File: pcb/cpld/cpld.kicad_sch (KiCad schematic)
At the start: 29 parts, among them J1 Micro_SD_Card_Det1, J2 Bus_ISA_8bit_AB_Rev0, J3 Atmel-JTAG-10, SW1 ADDR SEL, U1 ATF1504AS-xJx44, U2 AMS1117-3.3, U3 74LVC125, U4 74HCT688, X1 16MHz

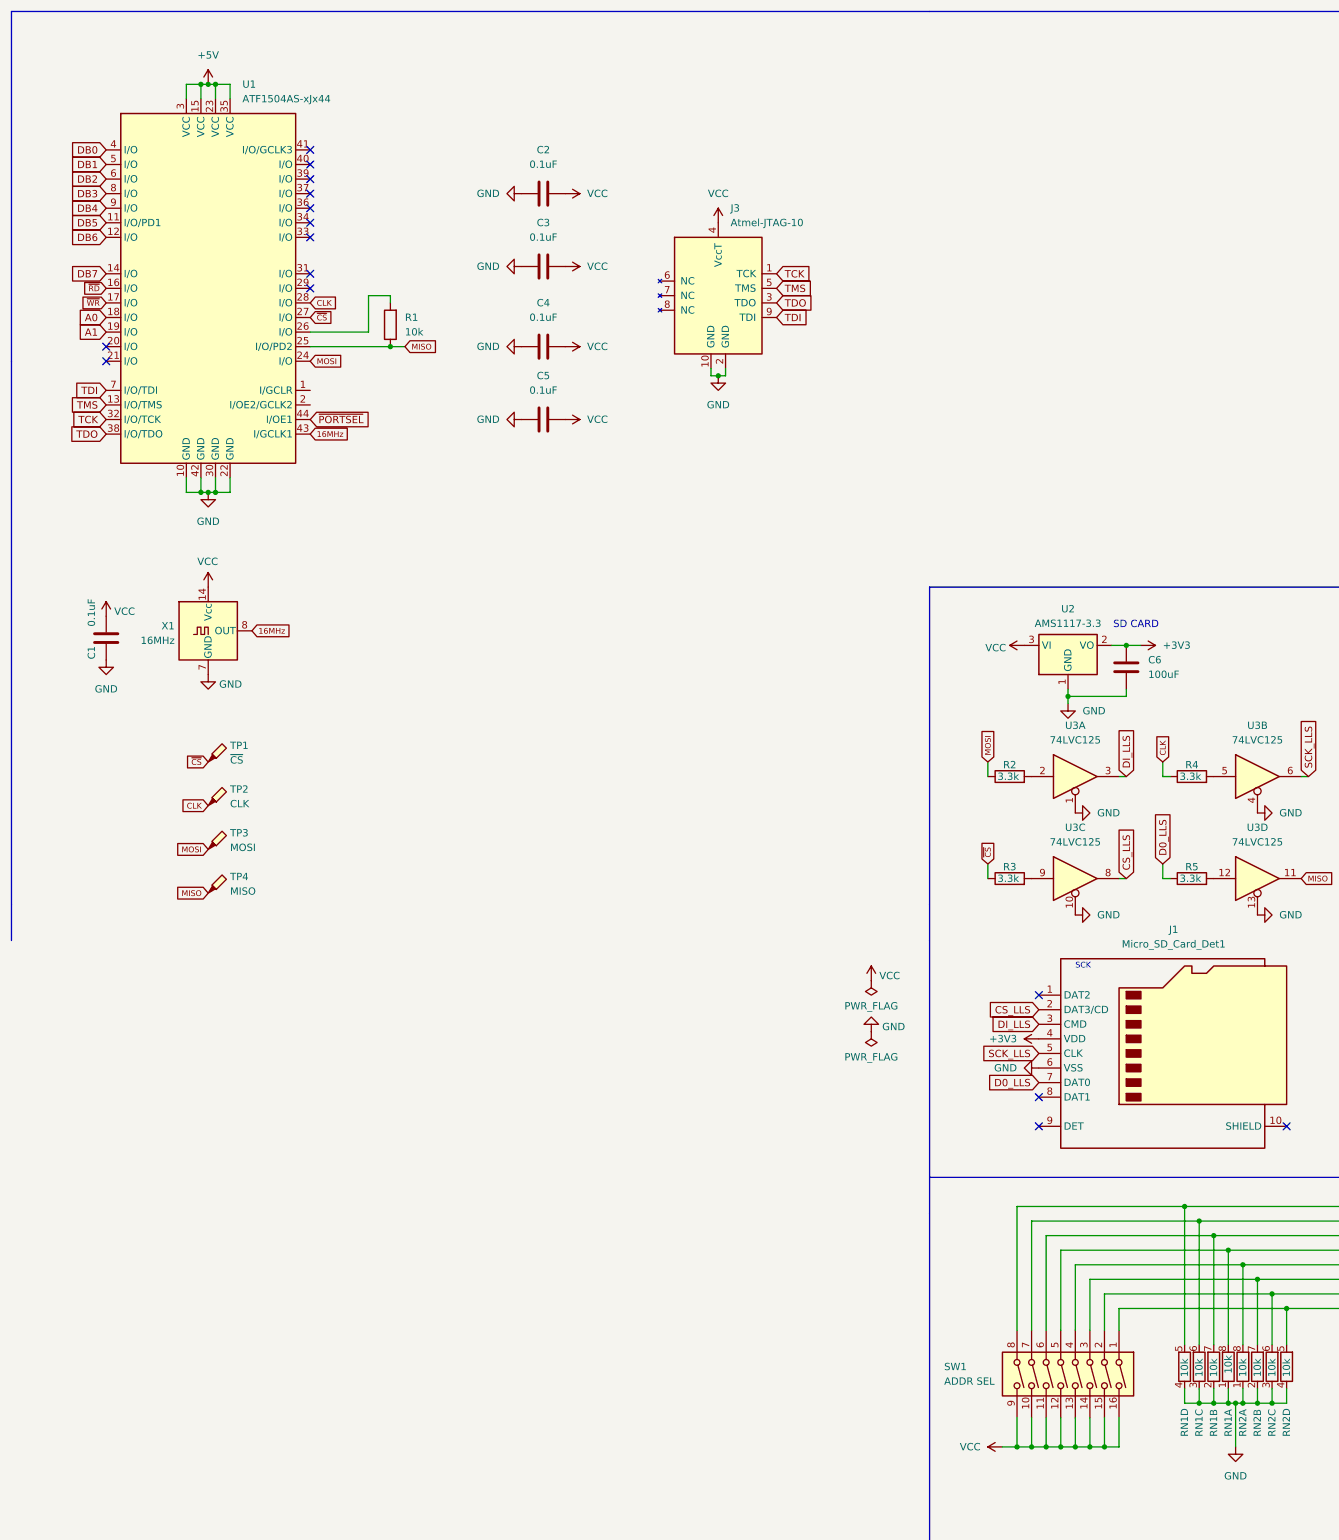
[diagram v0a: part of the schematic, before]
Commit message: Refactoring otternav and initial commit copying from HD to SD
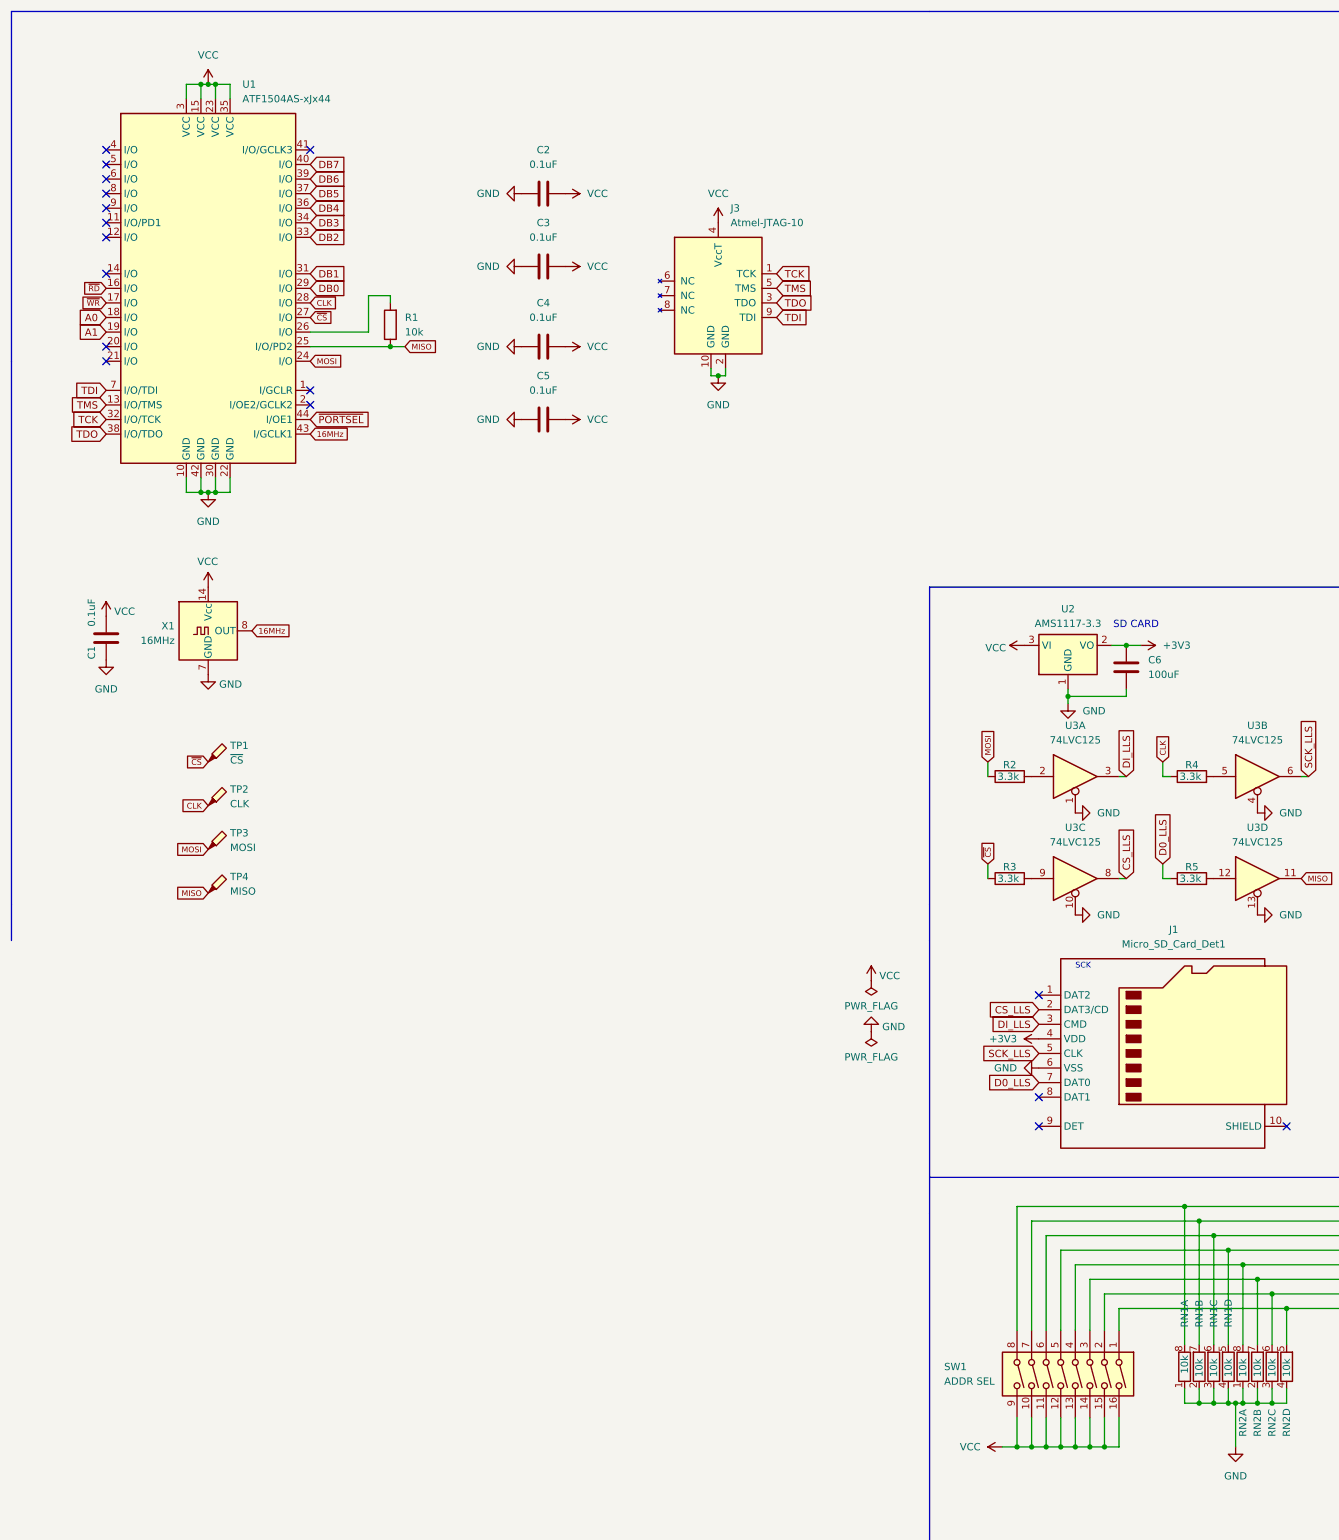
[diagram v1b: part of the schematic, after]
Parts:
- C2, C3, C4, C5: footprint Capacitor_THT:C_Disc_D5.0mm_W2.5mm_P5.00mm -> Capacitor_SMD:C_0805_2012Metric
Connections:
- net +5V is gone; now on net VCC: U1.15 (VCC), U1.23 (VCC), U1.3 (VCC), U1.35 (VCC)
- net DB0: now also U1.29 (I/O); no longer U1.4 (I/O)
- net DB1: now also U1.31 (I/O); no longer U1.5 (I/O)
- net DB2: now also U1.33 (I/O); no longer U1.6 (I/O)
- net DB3: now also U1.34 (I/O); no longer U1.8 (I/O)
- net DB4: now also U1.36 (I/O); no longer U1.9 (I/O)
- net DB5: now also U1.37 (I/O); no longer U1.11 (I/O/PD1)
- net DB6: now also U1.39 (I/O); no longer U1.12 (I/O)
- net DB7: now also U1.40 (I/O); no longer U1.14 (I/O)
- net at SW1.5, U4.9 (R3): now also RN1.5 (R4.2); no longer RN1.8 (R1.2)
- net at SW1.6, U4.7 (R2): now also RN1.6 (R3.2); no longer RN1.7 (R2.2)
- net at SW1.7, U4.5 (R1): now also RN1.7 (R2.2); no longer RN1.6 (R3.2)
- net at SW1.8, U4.3 (R0): now also RN1.8 (R1.2); no longer RN1.5 (R4.2)
- no-connect marks 51 -> 53
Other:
- moved on the sheet: RN1A, RN1B, RN1C, RN1D

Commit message: Refining CPLD card
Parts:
- added TP5, TP6: GND, TestPoint:TestPoint_Loop_D2.54mm_Drill1.5mm_Beaded, symbol Connector:TestPoint_Probe
- added unit 5 of U3
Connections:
- net +3V3: now also U3.14 (VCC)
- net GND: now also TP5.1, TP6.1, U3.7 (GND)
